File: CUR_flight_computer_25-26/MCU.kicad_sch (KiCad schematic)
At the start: 28 parts, among them SW1 GSPTS0018, SW2 SW_SPDT, U1 STM32H523VETx, Y1 16M18PX/XT324-10/10

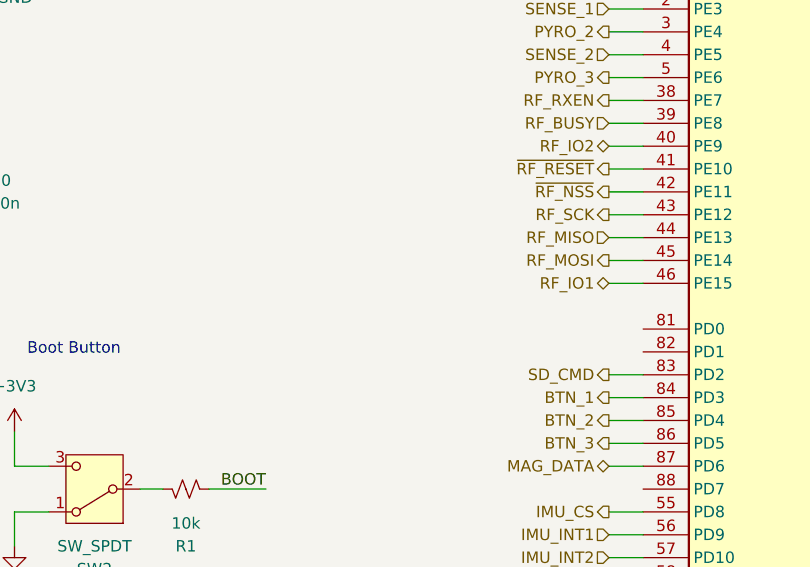
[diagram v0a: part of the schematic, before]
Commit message: updated rf module to ebyte-lora-400MM-22s
added footprint
added symbol
updates schematic
updated pcb
need to reroute
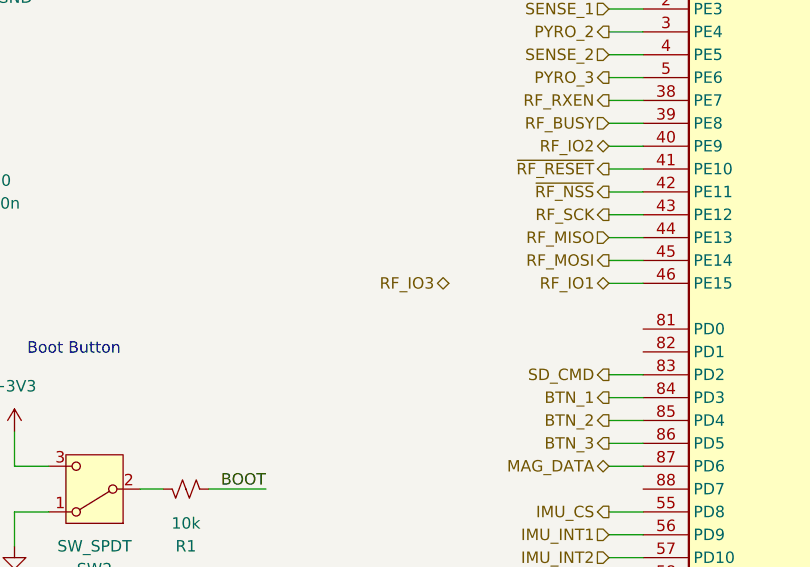
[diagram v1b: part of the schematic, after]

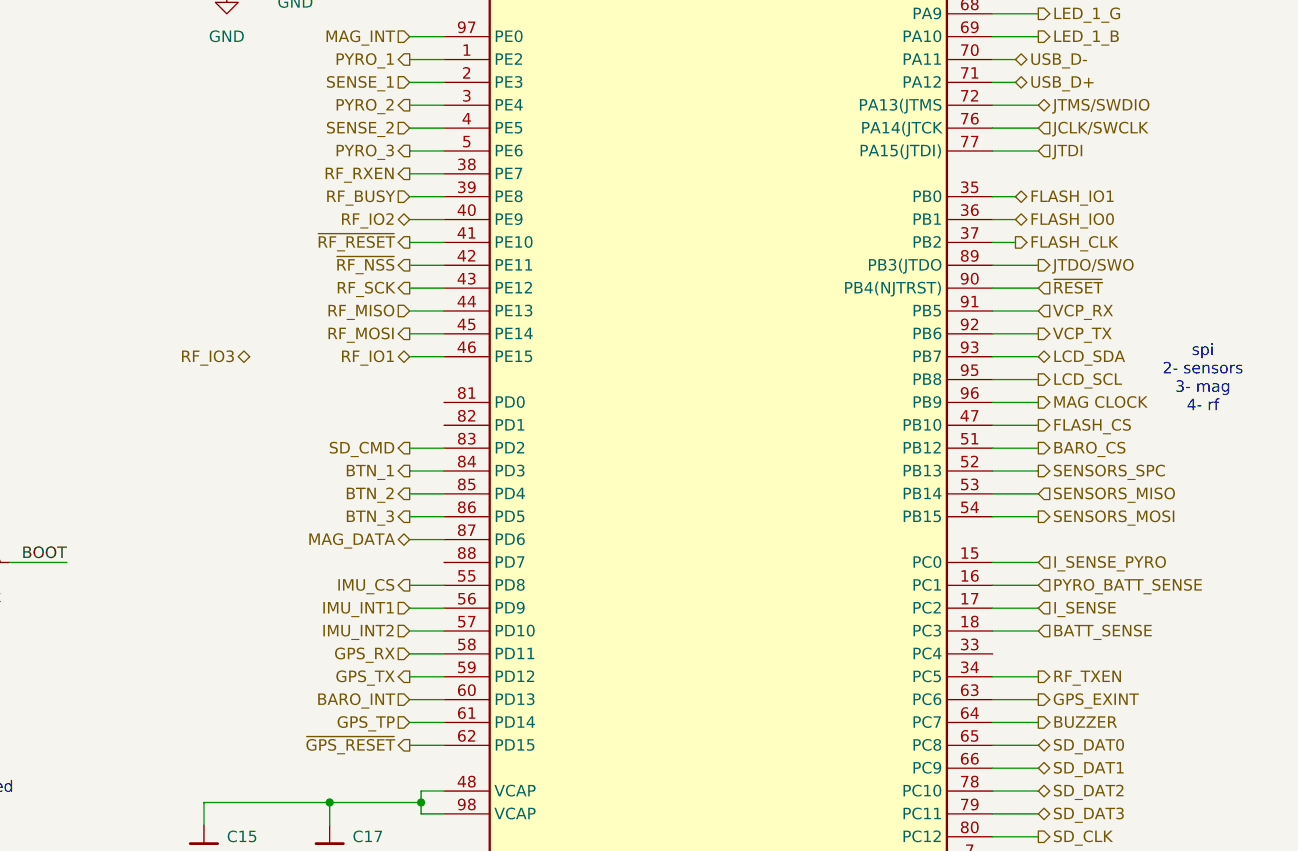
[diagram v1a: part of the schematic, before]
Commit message: routed much of back of the board
the flash will be awful
sd card, sensors, rf all routed
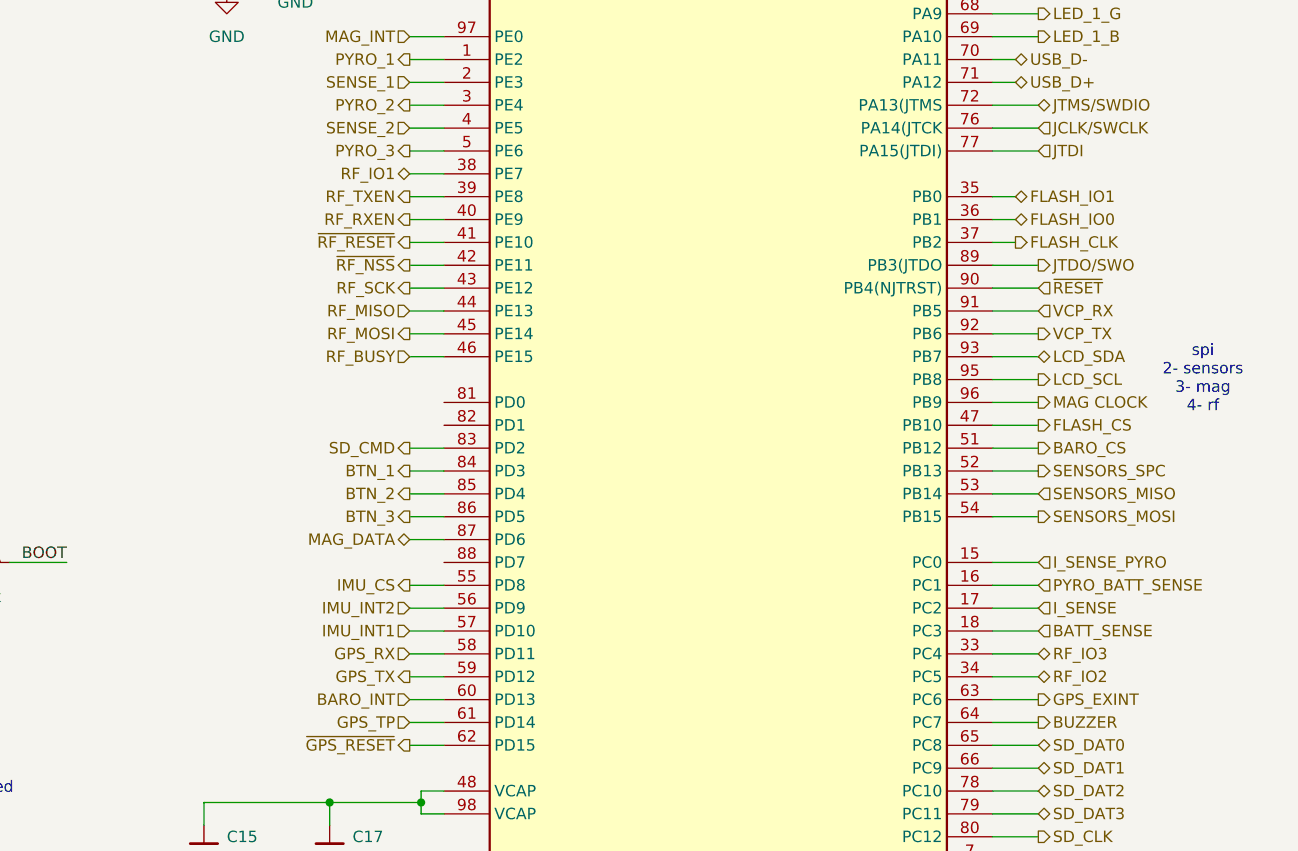
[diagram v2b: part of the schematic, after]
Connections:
- net IMU_INT1: now also U1.57 (PD10); no longer U1.56 (PD9)
- net IMU_INT2: now also U1.56 (PD9); no longer U1.57 (PD10)
- net RF_BUSY: now also U1.46 (PE15); no longer U1.39 (PE8)
- net RF_IO1: now also U1.38 (PE7); no longer U1.46 (PE15)
- net RF_IO2: now also U1.34 (PC5); no longer U1.40 (PE9)
- net RF_IO3: now also U1.33 (PC4)
- net RF_RXEN: now also U1.40 (PE9); no longer U1.38 (PE7)
- net RF_TXEN: now also U1.39 (PE8); no longer U1.34 (PC5)

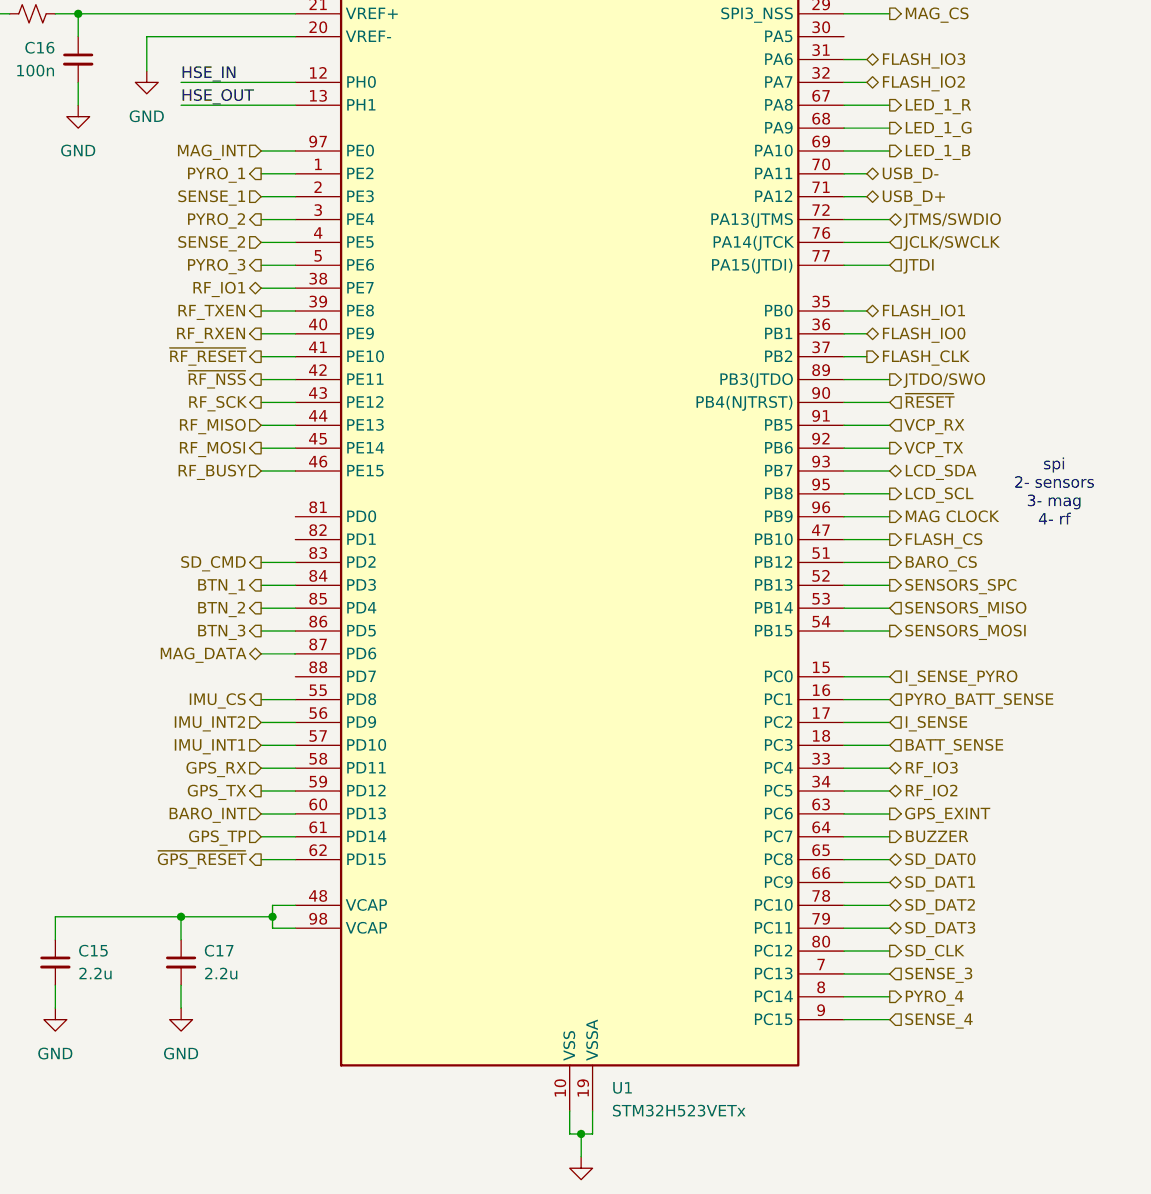
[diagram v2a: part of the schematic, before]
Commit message: routed hse, updates pyro pins order
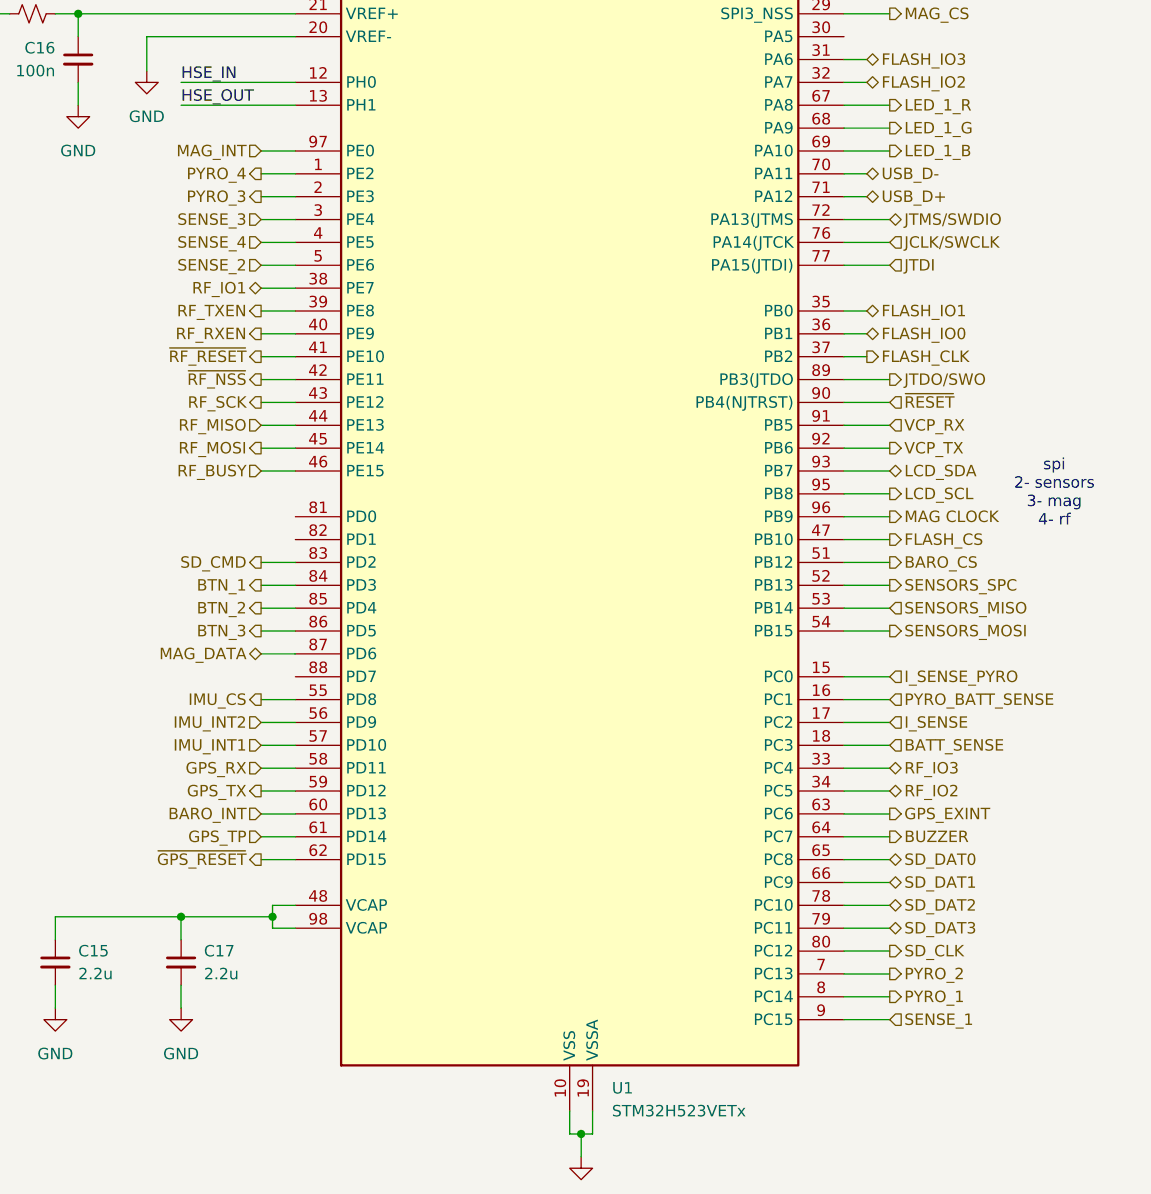
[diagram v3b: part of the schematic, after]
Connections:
- net PYRO_1: now also U1.8 (PC14); no longer U1.1 (PE2)
- net PYRO_2: now also U1.7 (PC13); no longer U1.3 (PE4)
- net PYRO_3: now also U1.2 (PE3); no longer U1.5 (PE6)
- net PYRO_4: now also U1.1 (PE2); no longer U1.8 (PC14)
- net SENSE_1: now also U1.9 (PC15); no longer U1.2 (PE3)
- net SENSE_2: now also U1.5 (PE6); no longer U1.4 (PE5)
- net SENSE_3: now also U1.3 (PE4); no longer U1.7 (PC13)
- net SENSE_4: now also U1.4 (PE5); no longer U1.9 (PC15)

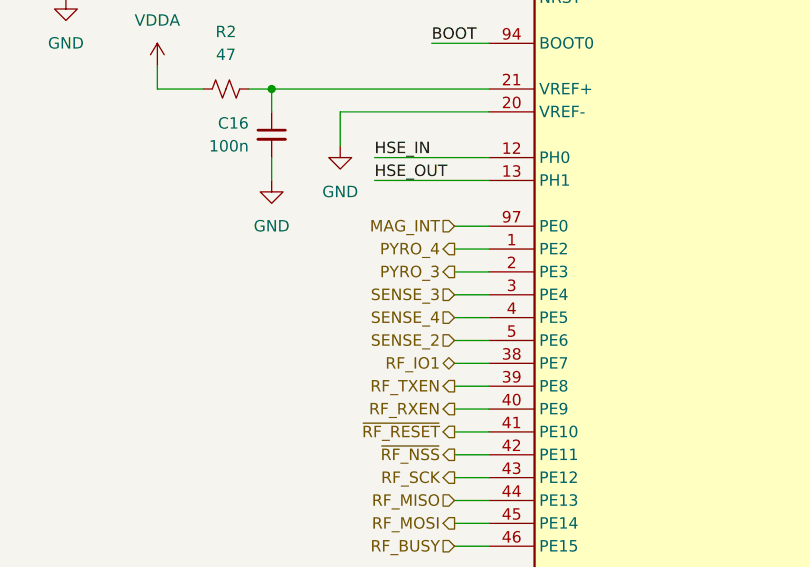
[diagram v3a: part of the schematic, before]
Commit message: routed pyro and sense lines
to do: buttons, lcd, buzzer, usb, boot switch, rf antenna
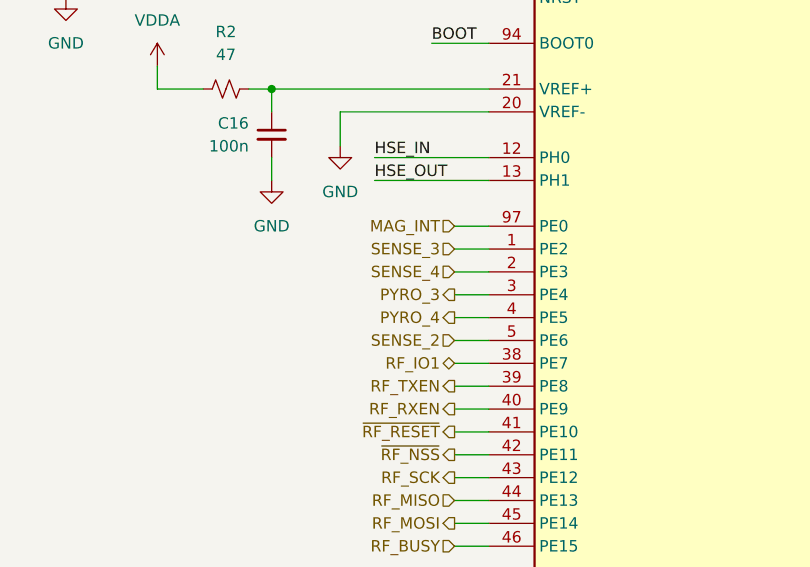
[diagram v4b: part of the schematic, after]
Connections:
- net PYRO_3: now also U1.3 (PE4); no longer U1.2 (PE3)
- net PYRO_4: now also U1.4 (PE5); no longer U1.1 (PE2)
- net SENSE_3: now also U1.1 (PE2); no longer U1.3 (PE4)
- net SENSE_4: now also U1.2 (PE3); no longer U1.4 (PE5)

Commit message: restart layout, downsize mounting holes
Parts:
- H1, H2, H3, H4: footprint MountingHole:MountingHole_3mm -> MountingHole:MountingHole_2.2mm_M2

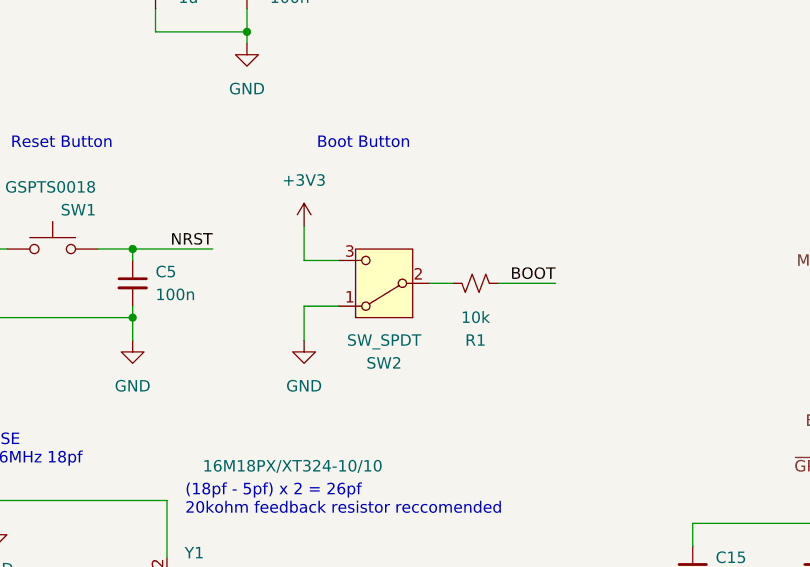
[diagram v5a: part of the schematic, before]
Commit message: Layout GPS and LoRa
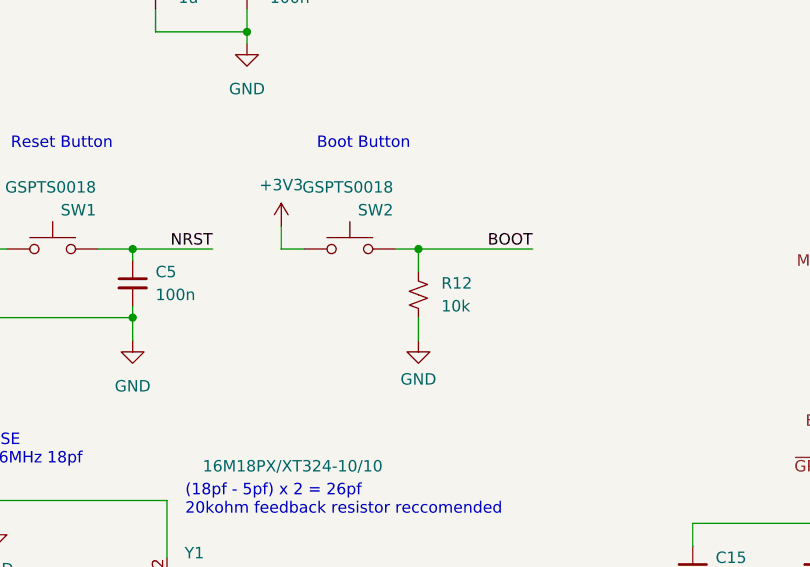
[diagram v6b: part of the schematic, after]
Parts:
- removed R1: 10k, Resistor_SMD:R_0603_1608Metric, symbol Device:R_Small_US
- removed SW2: SW_SPDT, SW_SameSky:SW_Samesky_SW_SLW-121456-3A-N-D, symbol Switch:SW_SPDT
- added R12: 10k, Resistor_SMD:R_0603_1608Metric, symbol Device:R_Small_US
- added SW2: GSPTS0018, PTS815_SJM_250_SMTR_LFS:SW_Push_PTS815_SJM_250_SMTR_LFS, symbol Switch:SW_Push
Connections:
- net +3V3: now also SW2.2
- net BOOT: now also R12.1, SW2.1
- net GND: now also R12.2

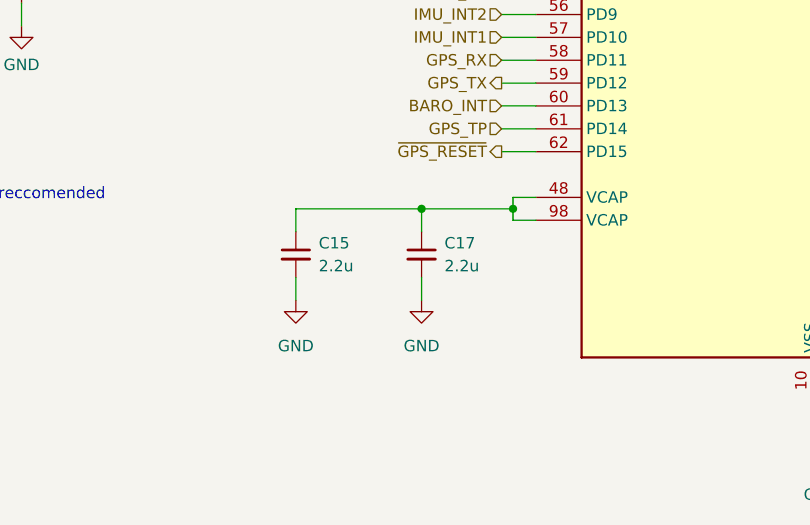
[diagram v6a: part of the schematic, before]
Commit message: Separate STM32 VCAP connection
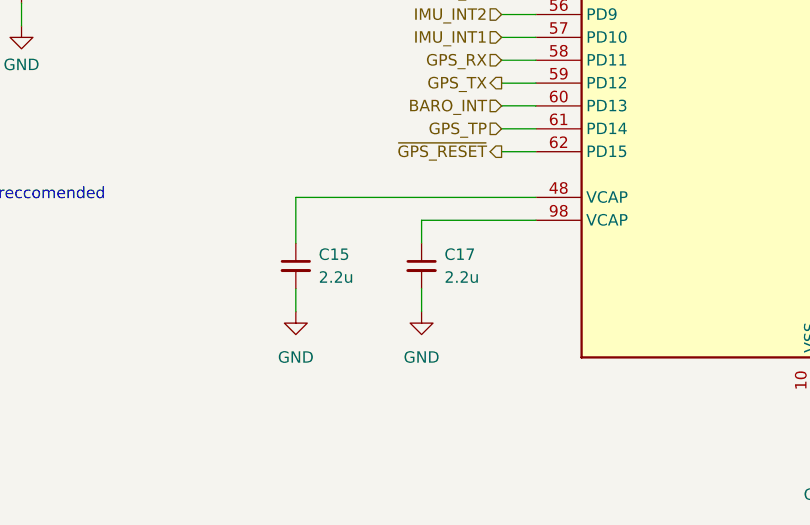
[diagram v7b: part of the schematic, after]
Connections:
- net at C15.1, U1.48 (VCAP): no longer C17.1, U1.98 (VCAP)
- new net: C17.1, U1.98 (VCAP)
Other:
- moved on the sheet: C15, C17
